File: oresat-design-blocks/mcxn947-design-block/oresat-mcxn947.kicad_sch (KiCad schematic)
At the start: 0 parts

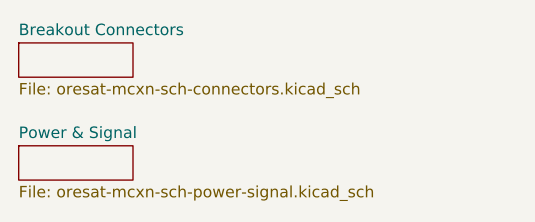
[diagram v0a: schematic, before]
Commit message: Cleanup of page names and put all power/connectors and signals on the same page facing the same way
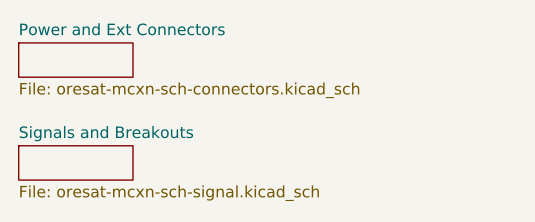
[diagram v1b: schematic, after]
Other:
- sheet Breakout Connectors renamed Power and Ext Connectors
- sheet Power & Signal renamed Signals and Breakouts
- sheet Signals and Breakouts: file oresat-mcxn-sch-power-signal.kicad_sch -> oresat-mcxn-sch-signal.kicad_sch
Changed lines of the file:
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@@
 			(color 0 0 0 0.0000)
 		)
-		(property "Sheetname" "Power & Signal"
+		(property "Sheetname" "Signals and Breakouts"
 			(at 204.47 122.4784 0)
 			(effects
@@
 			)
 		)
-		(property "Sheetfile" "oresat-mcxn-sch-power-signal.kicad_sch"
+		(property "Sheetfile" "oresat-mcxn-sch-signal.kicad_sch"
 			(at 204.47 127.5846 0)
 			(effects
@@
 			(color 0 0 0 0.0000)
 		)
-		(property "Sheetname" "Breakout Connectors"
+		(property "Sheetname" "Power and Ext Connectors"
 			(at 204.47 111.0484 0)
 			(effects
